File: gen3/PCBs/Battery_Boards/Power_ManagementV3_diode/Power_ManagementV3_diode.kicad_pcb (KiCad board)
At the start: 2 copper layers, 244 x 107 mm, 211 parts, among them J1 Conn_01x02_Pin, J10 via, J11 Conn_01x02_Pin, J12 Conn_01x02_Pin, J13 Conn_01x04_Pin, J14 Conn_01x08, J15 Conn_01x08, J16 Conn_01x02_Pin, J17 FPGA MOUNT, J18 Conn_01x04_Socket, J19 via, J2 Conn_01x02_Pin, J20 via, J3 Conn_01x08, J4 Conn_01x08, J5 Conn_01x02_Pin, J6 Conn_01x02_Pin, J7 USB_A_Stacked, J8 SBH11-PBPC-D10-ST-BK, J9 Conn_01x04_Pin, Q1 MCTL160N15Y-TP, Q2 MCTL160N15Y-TP, Q3 MCTL160N15Y-TP, Q4 MCTL160N15Y-TP, Q5 MCTL160N15Y-TP, Q6 MCTL160N15Y-TP, U1 STPS5045SG-TR, U10 SN74HC132PWR, U11 SN74LVC1G373DCKR, U12 MCP6564-E/ST, U13 STPS5045SG-TR, U14 MCP9808_MSOP, U15 BA033CC0FP-E2, U16 MCP9808_MSOP, U2 STPS5045SG-TR, U3 LTC1255CS8-PBF, U4 BA033CC0FP-E2, U5 ACS758LCB-100U-PFF-T, U6 SN74HC132PWR, U7 74VHC21FT, U8 SN74HC132PWR, U9 SN74HC132PWR

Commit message: Add shared robosub KiCad libraries, importorted 5v regulator, made some changes to battery management board
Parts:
- removed U13: STPS5045SG-TR, Imported_Footprints:D2PAK_STM
- removed U15: BA033CC0FP-E2, Imported_Footprints:TO252-3_ROM
- removed U16: MCP9808_MSOP, Package_SO:MSOP-8_3x3mm_P0.65mm
- H8 (x2), J11, J12: moved to B.Cu
- J13: value Conn_01x04_Pin -> Conn_01x02_Pin; footprint Imported_Footprints:CONN_SD-43045-008_04_MOL -> Connector_AMASS:AMASS_XT30PW-F_1x02_P2.50mm_Horizontal
- moved R36 249.1 mm to (-29.0, 259.0), turned to -90 degrees
- moved R35 248.7 mm to (-31.0, 259.0), turned to 90 degrees
- moved R33 243.4 mm to (-29.0, 254.9), turned to -90 degrees
- moved R34 242.9 mm to (-31.0, 254.9), turned to 90 degrees
- moved J14 238.4 mm to (-25.9, 250.7), turned to 0 degrees
- moved R32 237.8 mm to (-29.0, 250.9), turned to 90 degrees
- moved R31 237.3 mm to (-30.9, 250.9), turned to -90 degrees
- moved J15 235.5 mm to (-38.6, 250.7), turned to 0 degrees
- moved H8 169.1 mm to (126.4, 211.0), turned to -90 degrees
- moved H8 140.5 mm to (40.0, 197.0), turned to -90 degrees
- moved H6 125.4 mm to (29.3, 211.0), turned to -90 degrees
- moved H9 117.3 mm to (126.4, 138.0), turned to -90 degrees
- moved J18 102.3 mm to (71.3, 154.0)
- moved J13 81.3 mm to (46.0, 137.0), turned to 180 degrees
- moved J12 73.6 mm to (56.4, 147.8), turned to 0 degrees
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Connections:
- C13 pad 1: +3.3V -> +3.3V_diode
- C14 pad 1: +3.3V -> +3.3V_diode
- J13 pad 1: unconnected-(J13-Pin_1-Pad1) -> /SCL
- J13 pad 2: GND_bak -> /SDA
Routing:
- net +TEMP_BATT: track 105.4 -> 0.00 mm, vias 2 -> 0
- net /SDA: track 88.6 -> 0.00 mm
- net +3.3V: track 363.1 -> 281.6 mm
- net /SCL: track 64.5 -> 0.00 mm
- net +BATT: track 55.1 -> 0.00 mm, vias 2 -> 0
- net +EXT_LV_SUPPLY: track 39.5 -> 0.00 mm, vias 1 -> 0
- net GND_bak: track 30.9 -> 0.00 mm, vias 3 -> 0
- net Net-(J14-Pin_2): track 6.21 -> 0.00 mm
- net Net-(J14-Pin_3): track 6.02 -> 0.00 mm
- net Net-(J14-Pin_1): track 5.48 -> 0.00 mm
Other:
- board size 244 x 107 mm -> 273.6 x 179 mm
- board text added: "ADC SPLITTER"
- board text added: "BATTERY OUT"
- board text added: "DO NOT LEAVE CONNECTED"
- board text added: "HOTSWAP"
- board text added: "I2C"
- board text added: "MAIN BATTERY"
- board text added: "SCL"
- board text added: "SDA"

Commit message: added caps to micro breakout
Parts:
- removed R40: 20k, Resistor_SMD:R_0805_2012Metric_Pad1.20x1.40mm_HandSolder
- added C15: 10uF, Capacitor_SMD:C_0805_2012Metric_Pad1.18x1.45mm_HandSolder, F.Cu at (76.9, 144.6)
- added C16: 0.1u, Capacitor_SMD:C_0805_2012Metric_Pad1.18x1.45mm_HandSolder, F.Cu at (51.0, 187.1)
- added C17: 100nF, Capacitor_SMD:C_0805_2012Metric_Pad1.18x1.45mm_HandSolder, F.Cu at (56.1, 187.7)
- added C18: 1µF, Capacitor_SMD:C_0805_2012Metric_Pad1.18x1.45mm_HandSolder, F.Cu at (54.1, 187.7)
- added C19: 10uF, Capacitor_SMD:C_0805_2012Metric_Pad1.18x1.45mm_HandSolder, F.Cu at (81.2, 144.5)
- added C20: 1uF, Capacitor_SMD:C_0805_2012Metric_Pad1.18x1.45mm_HandSolder, F.Cu at (79.1, 144.5)
- added D15: SS54, Diode_SMD:D_SMA_Handsoldering, F.Cu at (74.1, 136.4)
- added D16: SS54, Diode_SMD:D_SMA_Handsoldering, F.Cu at (74.3, 140.5)
- added J21: Conn_01x02_Pin, Connector_AMASS:AMASS_XT60PW-F_1x02_P7.20mm_Horizontal, F.Cu at (32.0, 171.5)
- added J22: Conn_01x02_Pin, Connector_AMASS:AMASS_XT60PW-F_1x02_P7.20mm_Horizontal, F.Cu at (32.0, 154.7)
- added Q7: L78M05ABDT-TR, robosub_footprints:TO-252-2_L6.5-W6.1-P4.58-LS10.0-TL, F.Cu at (84.5, 138.7)
- added U13: STPS5045SG-TR, Imported_Footprints:D2PAK_STM, F.Cu at (70.2, 165.0)
- added U15: AMS1117-3.3, Package_TO_SOT_SMD:SOT-223-3_TabPin2, F.Cu at (87.7, 147.2)
- added U16: MCP9808_MSOP, Package_SO:MSOP-8_3x3mm_P0.65mm, F.Cu at (38.8, 165.7)
- added U17: ACS758LCB-100U-PFF-T, Imported_Footprints:Allegro_MicroSystems,_LLC-CB-5-PFF-0-0-MFG, F.Cu at (52.0, 174.9)
- added U18: ACS758LCB-100U-PFF-T, Imported_Footprints:Allegro_MicroSystems,_LLC-CB-5-PFF-0-0-MFG, F.Cu at (18.0, 26.1)
- R29, R37, R39: value 10k -> 0R
- R30, R38: value 20k -> 0R
- moved C13 217.2 mm to (86.8, 153.8), turned to -90 degrees
- moved R39 217.0 mm to (70.1, 190.1)
- moved C14 215.8 mm to (88.9, 153.7), turned to -90 degrees
- moved R27 213.7 mm to (58.1, 187.7), turned to -90 degrees
- moved R28 212.0 mm to (60.0, 187.7), turned to 90 degrees
- moved C12 210.0 mm to (83.2, 144.6), turned to -90 degrees
- moved R38 208.2 mm to (70.1, 192.1)
- moved R29 192.7 mm to (39.6, 179.4)
- moved R30 188.3 mm to (39.6, 177.5)
- moved R41 183.3 mm to (39.6, 173.3)
- moved R37 181.8 mm to (39.6, 175.4)
- moved R32 129.8 mm to (76.3, 174.9), turned to -90 degrees
- moved J14 129.6 mm to (79.1, 174.7)
- moved J15 129.6 mm to (66.4, 174.7)
- moved R31 129.6 mm to (74.1, 174.9)
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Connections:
- C12 pad 1: +EXT_LV_SUPPLY -> +5V_
- C13 pad 1: +3.3V_diode -> +3.3V_
- C14 pad 1: +3.3V_diode -> +3.3V_
- CR1 pad 3: +BATT -> +BATT_main
- D3 pad 2: +BATT -> +BATT_main
- J10 pad 1: +BATT -> +BATT_main
- J14 pad 4: unconnected-(J14-Pin_4-Pad4) -> current_sensor_3v3
- J15 pad 1: +3.3V -> +3.3V_
- J15 pad 5: +3.3V -> +3.3V_
- J15 pad 7: unconnected-(J15-Pin_7-Pad7) -> Net-(J15-Pin_7)
- J15 pad 8: unconnected-(J15-Pin_8-Pad8) -> Net-(J15-Pin_8)
- J16 pad 2: +BATT -> +BATT_out
- J5 pad 2: +BATT -> +BATT_main
- J6 pad 2: +BATT -> +BATT_main
- JP12 pad 2: +BATT -> +BATT_main
- R14 pad 1: +BATT -> +BATT_main
- R27 pad 1: Net-(U16-SDA) -> current_sensor_5v
- R27 pad 2: /SDA -> current_sensor_3v3
- R28 pad 1: /SDA -> current_sensor_3v3
- R29 pad 2: /SCL -> +3.3V_
- R30 pad 1: /SCL -> Net-(U16-A1)
- R30 pad 2: GND_bak -> +3.3V_
- R37 pad 2: /SDA -> +3.3V_
- R38 pad 1: /SDA -> Net-(J15-Pin_8)
- R38 pad 2: GND_bak -> +3.3V_
- R39 pad 1: Net-(J15-Pin_3) -> Net-(J15-Pin_7)
- R39 pad 2: /SCL -> +3.3V_
- R41 pad 1: +3.3V -> +3.3V_
- U5 pad 5: +BATT -> +BATT_main
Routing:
- net +3.3V_: track 0.00 -> 136.2 mm
- net +5V_: track 0.00 -> 123.9 mm
- net /SCL: track 0.00 -> 75.3 mm
- net /SDA: track 0.00 -> 68.2 mm
- net +TEMP_BATT: track 0.00 -> 63.3 mm
- net GND_bak: track 0.00 -> 51.1 mm, vias 0 -> 8
- net +EXT_LV_SUPPLY: track 0.00 -> 29.5 mm
- net current_sensor_3v3: track 0.00 -> 27.1 mm
- net +BATT: track 0.00 -> 22.7 mm
- net Net-(U16-A2): track 0.00 -> 12.8 mm
- net Net-(D15-K): track 0.00 -> 11.8 mm
- net Net-(U16-A1): track 0.00 -> 10.8 mm
- net Net-(U16-A0): track 0.00 -> 8.60 mm
- net current_sensor_5v: track 0.00 -> 6.24 mm
- net Net-(J14-Pin_2): track 0.00 -> 6.21 mm
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- added copper zone on B.Cu, net +BATT_main
- added copper zone on F.Cu, net +BATT_main
- added copper zone on B.Cu, net +BATT_out
- added copper zone on F.Cu, net +BATT_out
- added copper zone on F.Cu, net GND_bak
- removed copper zone on B.Cu, net +BATT
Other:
- board size 273.6 x 179 mm -> 277 x 174 mm
- board text added: "68mm"
- board text added: "82mm"

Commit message: bms board finished
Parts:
- removed 1A1, 1B1, 1Y1, 2A2, 2B2, 2Y1, 3A2, 3B2, 3Y1, 4A1, 4B1, 4Y1, TP13, TP14, TP2, TP3, TP4, TP5, TP6, TP8, TP9: TestPoint, TestPoint:TestPoint_Pad_1.0x1.0mm
- removed C1: 10uF, Imported_Footprints:CAP_EEE-1CA100SR_PAN
- removed C10, C11: 10,000uF, Capacitor_THT:CP_Radial_D16.0mm_P7.50mm
- removed C2, C3, C4, C5: 10uF, Capacitor_SMD:C_0805_2012Metric_Pad1.18x1.45mm_HandSolder
- removed C6: 1uF, Capacitor_SMD:C_0805_2012Metric_Pad1.18x1.45mm_HandSolder
- removed C7: 0.1u, Capacitor_SMD:C_0805_2012Metric_Pad1.18x1.45mm_HandSolder
- removed C8: 100nF, Capacitor_SMD:C_0805_2012Metric_Pad1.18x1.45mm_HandSolder
- removed C9: 1µF, Capacitor_SMD:C_0805_2012Metric_Pad1.18x1.45mm_HandSolder
- removed CR1: SBRT15U50SP5-13, Imported_Footprints:POWERDI5_DIO
- removed D1, D2: D_Zener, Imported_Footprints:1N5242B
- removed D10, D11, D12, D13, D14, D4, D5, D6, D7, D8, D9: GreenLED, LED_SMD:LED_0603_1608Metric_Pad1.05x0.95mm_HandSolder
- removed D3: TVS, Diode_SMD:D_SMA
- removed H1, H2, H3, H4: MountingHole, MountingHole:MountingHole_3.2mm_M3
- removed the H6 at (278.0, 139.1)
- removed the H7 at (205.0, 139.0)
- removed the H8 at (278.0, 42.0)
- removed the H9 at (205.0, 42.0)
- removed J1, J2: Conn_01x02_Pin, Connector_AMASS:AMASS_XT60IPW-M_1x03_P7.20mm_Horizontal
- removed J10: via, MountingHole:MountingHole_4.3x6.2mm_M4_Pad_Via
- removed J17: FPGA MOUNT, Connector_PinHeader_2.54mm:PinHeader_2x02_P2.54mm_Vertical
- removed J19, J20: via, MountingHole:MountingHole_3.7mm_Pad_Via
- removed J3, J4: Conn_01x08, Connector_PinHeader_2.54mm:PinHeader_1x08_P2.54mm_Vertical
- removed J5: Conn_01x02_Pin, Connector_AMASS:AMASS_XT60PW-F_1x02_P7.20mm_Horizontal
- removed J6: Conn_01x02_Pin, Connector_AMASS:AMASS_XT30PW-F_1x02_P2.50mm_Horizontal
- removed J7: USB_A_Stacked, Connector_USB:USB_A_Wuerth_61400826021_Horizontal_Stacked
- removed J8: SBH11-PBPC-D10-ST-BK, Imported_Footprints:SULLINS_SBH11-PBPC-D10-ST-BK
- removed J9: Conn_01x04_Pin, Imported_Footprints:CONN_SD-43045-008_04_MOL
- removed JP1, JP3: SolderJumper_2_Bridged, Jumper:SolderJumper-2_P1.3mm_Bridged2Bar_RoundedPad1.0x1.5mm
- removed JP10, JP11, JP13, JP14, JP15, JP16, JP17, JP18, JP19, JP20, JP25, JP27: Jumper_2_Bridged, Jumper:SolderJumper-2_P1.3mm_Bridged2Bar_RoundedPad1.0x1.5mm
- removed JP12: Jumper_2_Open, Imported_Footprints:KEYSTONE_5102
- removed JP2: SolderJumper_2_Open, Jumper:SolderJumper-2_P1.3mm_Open_RoundedPad1.0x1.5mm
- removed JP21, JP23, JP26: Jumper_2_Open, Jumper:SolderJumper-2_P1.3mm_Open_RoundedPad1.0x1.5mm
- removed JP28, JP8, JP9: Jumper_3_Bridged12, Jumper:SolderJumper-3_P1.3mm_Bridged2Bar12_RoundedPad1.0x1.5mm
- removed JP6, JP7: ~, Jumper:SolderJumper-2_P1.3mm_Bridged2Bar_RoundedPad1.0x1.5mm
- removed LED1, LED10, LED11, LED12, LED13, LED14, LED15, LED16, LED17, LED18, LED19, LED2, LED20, LED21, LED22, LED23, LED24, LED25, LED26, LED27, LED28, LED29, LED3, LED4, LED5, LED6, LED7, LED8, LED9: 1655, LED_SMD:LED_LiteOn_LTST-E563C_PLCC4_5.0x5.0mm_P3.2mm_HandSoldering
- removed PM1, PM2: LMS78, Imported_Footprints:LMS78
- removed Q1, Q2, Q3, Q4, Q5, Q6: MCTL160N15Y-TP, Imported_Footprints:TOLL-8L_MCC
- removed R1, R6: 50k, Resistor_SMD:R_0805_2012Metric_Pad1.20x1.40mm_HandSolder
- removed R10, R42, R43, R44, R45, R9: 0R, Resistor_SMD:R_0805_2012Metric_Pad1.20x1.40mm_HandSolder
- removed R11, R12, R17, R18, R19, R20, R22, R23, R24: 100, Resistor_SMD:R_0402_1005Metric
- removed R13: 2.2k, Resistor_SMD:R_0805_2012Metric_Pad1.20x1.40mm_HandSolder
- removed R14: 0.5 Ohm 25W, Imported_Footprints:TO508P1229X317-3N
- removed R15: 3.9k, Resistor_SMD:R_0805_2012Metric_Pad1.20x1.40mm_HandSolder
- removed R16, R2, R3, R7, R8: 10k, Resistor_SMD:R_0805_2012Metric_Pad1.20x1.40mm_HandSolder
- removed R21: 100 Ohm, Imported_Footprints:2506_8x_Resistor_Array
- removed R25: 15k, Resistor_SMD:R_0402_1005Metric
- removed R26: 1.5k, Resistor_SMD:R_0402_1005Metric
- removed R4, R5: 100k, Resistor_SMD:R_0805_2012Metric
- removed S1: 100SP1T1B4M2QE, Imported_Footprints:SW_100SP1T1B4M2QE
- removed TH1, TH2: Thermistor_US, Resistor_SMD:R_0805_2012Metric
- removed U1, U13, U2: STPS5045SG-TR, Imported_Footprints:D2PAK_STM
- removed U10, U6, U8, U9: SN74HC132PWR, eli_custom_footprint_lib:SOP65P640X120-14N
- removed U11: SN74LVC1G373DCKR, Imported_Footprints:SN74LVC
- removed U12: MCP6564-E/ST, footprints:TSSOP14_MC_MCH
- removed U14: MCP9808_MSOP, Package_SO:MSOP-8_3x3mm_P0.65mm
- removed U3: LTC1255CS8-PBF, Imported_Footprints:LTC1255
- removed U4: BA033CC0FP-E2, Imported_Footprints:TO252-3_ROM
- removed U5: ACS758LCB-100U-PFF-T, Imported_Footprints:Allegro_MicroSystems,_LLC-CB-5-PFF-0-0-MFG
- removed U7: 74VHC21FT, Imported_Footprints:TSSOP14B
- removed VR1, VR2: 3296W-1-103RLF, Imported_Footprints:TRIM_3296W-1-103RLF
- C16: value 0.1u -> 0.1uF
- U18: value ACS758LCB-100U-PFF-T -> SRT60L100DC-R; footprint Imported_Footprints:Allegro_MicroSystems,_LLC-CB-5-PFF-0-0-MFG -> Package_TO_SOT_SMD:TO-263-2
- moved U18 237.7 mm to (246.6, 91.2), turned to 180 degrees
- moved C17 192.3 mm to (233.7, 113.9)
- moved C18 192.3 mm to (231.7, 113.8)
- moved D16 192.3 mm to (251.9, 66.7)
- moved H8 192.3 mm to (285.6, 132.2)
- moved R37 192.3 mm to (217.2, 101.6)
- moved U16 192.3 mm to (216.4, 91.9)
- moved C12 192.3 mm to (260.8, 70.8)
- moved C13 192.3 mm to (264.4, 80.0)
- moved C14 192.3 mm to (266.5, 79.8)
- moved C15 192.3 mm to (254.5, 70.8)
- moved C19 192.3 mm to (258.8, 70.7)
- moved D15 192.3 mm to (251.7, 62.6)
- moved H6 192.3 mm to (203.5, 132.2)
- moved H7 192.3 mm to (203.6, 64.2)
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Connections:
- U18 pad 1: unconnected-(U18-VCC-Pad1) -> +EXT_LV_SUPPLY
- U18 pad 2: unconnected-(U18-GND-Pad2) -> +BATT
- U18 pad 3: unconnected-(U18-VIOUT-Pad3) -> +EXT_LV_SUPPLY
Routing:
- net +3.3V: track 281.6 -> 0.00 mm, vias 13 -> 0
- net ISample5V: track 260.2 -> 0.00 mm
- net +5V: track 231.1 -> 0.00 mm, vias 2 -> 0
- net Batt2Gate: track 198.2 -> 0.00 mm, vias 6 -> 0
- net I2C1_SDA: track 191.8 -> 0.00 mm
- net +BATT2: track 171.3 -> 0.00 mm, vias 2 -> 0
- net I2C1_SCL: track 167.1 -> 0.00 mm
- net +BATT1: track 133.4 -> 0.00 mm, vias 2 -> 0
- net Batt1Enable: track 125.4 -> 0.00 mm
- net Batt1Gate: track 111.9 -> 0.00 mm
- net /ENABLE_BATT2: track 86.2 -> 0.00 mm, vias 2 -> 0
- net +VregDiode: track 75.9 -> 0.00 mm, vias 3 -> 0
- net VSampleBatt1: track 74.9 -> 0.00 mm, vias 8 -> 0
- net VSampleBatt2: track 70.3 -> 0.00 mm, vias 5 -> 0
- net -BATT1: track 69.8 -> 0.00 mm, vias 19 -> 0
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- removed copper zone on F.Cu, net +BATT1
- removed copper zone on F.Cu, net +BATT2
- removed copper zone on F.Cu, net +BATTHall
- removed copper zone on B.Cu, net +BATT_main
- removed copper zone on F.Cu, net +BATT_main
- removed copper zone on B.Cu, net -BATT1
- removed copper zone on F.Cu, net -BATT1
- removed copper zone on F.Cu, net Capacitors
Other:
- board size 277 x 174 mm -> 92 x 78 mm
- board text added: "BUCK CONVERTER HERE"
- board text removed: "+Vo"
- board text removed: "ADC Splitter"
- board text removed: "BATT 1 ENABLE"
- board text removed: "BATT 1 GATE"
- board text removed: "BATT 2 GATE"
- board text removed: "BATT1"
- board text removed: "BATT1 FIX POINT"
- board text removed: "BATT2"
- board text removed: "BATT2 FIX POINT"
- board text removed: "Batt1En"
- board text removed: "Batt1UVP"
- board text removed: "Batt2En"
- board text removed: "Batt2UVP"
- board text removed: "Enable"
- board text removed: "ExtKill"
- board text removed: "GATE DRIVER"
- board text removed: "GROUND"
- board text removed: "KillStatus"
- board text removed: "OCPLatch"
- board text removed: "Said Vassili on the first iteration of this..."
- board text removed: "Stanford Robosub Power Management"
- board text removed: "Switch"
- board text removed: "TVS DIODE"
- board text removed: "Vin"
- board text removed: "ballast resistance 7x14mm ~ 1mOhm"
- board text removed: "zener protection diodes (Vgs > 12V) the driver drives until the clamp is satisfied"
- board text removed: "{dblquote}Survival is the ability to swim in strange water{dblquote}"

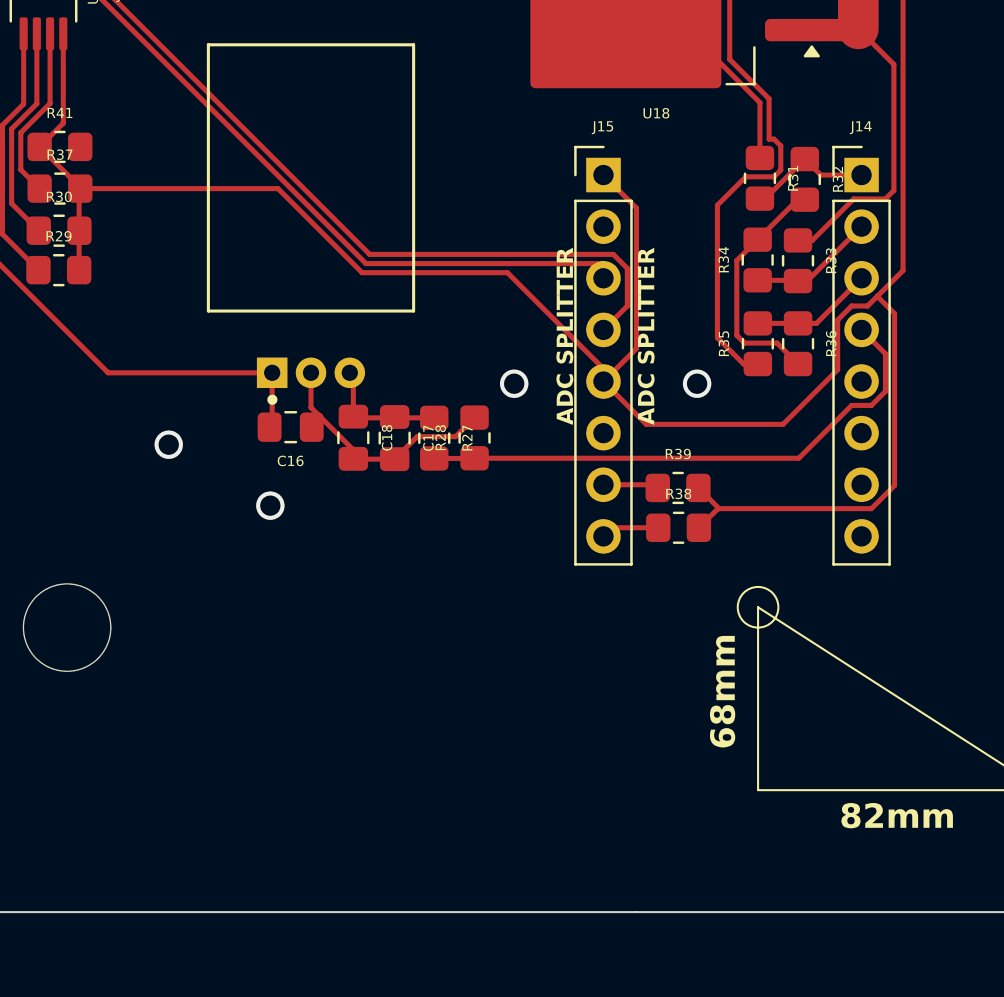
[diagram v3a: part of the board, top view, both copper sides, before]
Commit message: added to_order
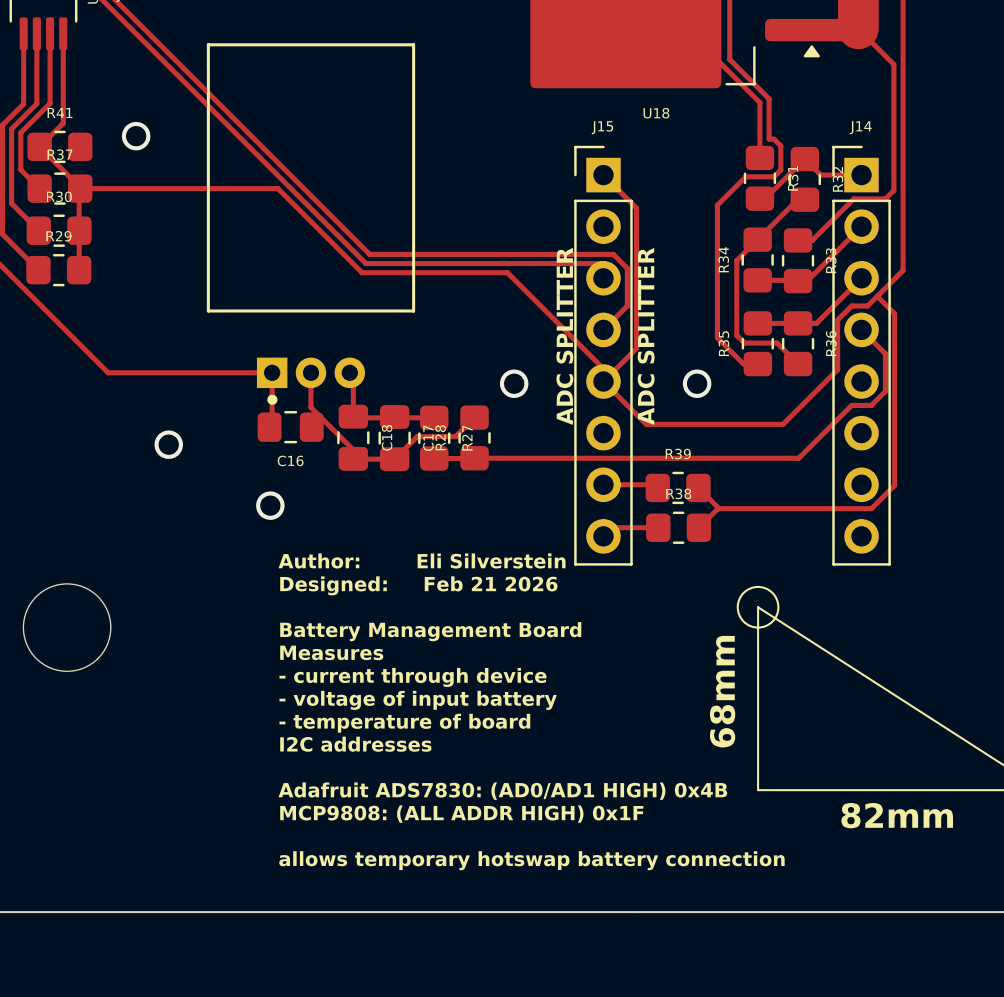
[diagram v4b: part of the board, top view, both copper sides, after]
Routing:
- net GND_bak: vias 8 -> 9
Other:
- board text added: "Author: Eli Silverstein Designed: Feb 21 2026 Battery Management Board Measures - current through device - voltage of input battery - temperature of board I2C addresses Adafruit ADS7830: (AD0/AD1 HIGH) 0x4B MCP9808: (ALL ADDR HIGH) 0x1F allows temporary hotswap battery connection"
